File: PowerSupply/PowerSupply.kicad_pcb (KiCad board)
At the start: 2 copper layers, 100 x 58 mm, 26 parts, among them J1 AC+, J2 AC-, J3 POWER, U1 LM317_SOT-223, U2 LM337_SOT223

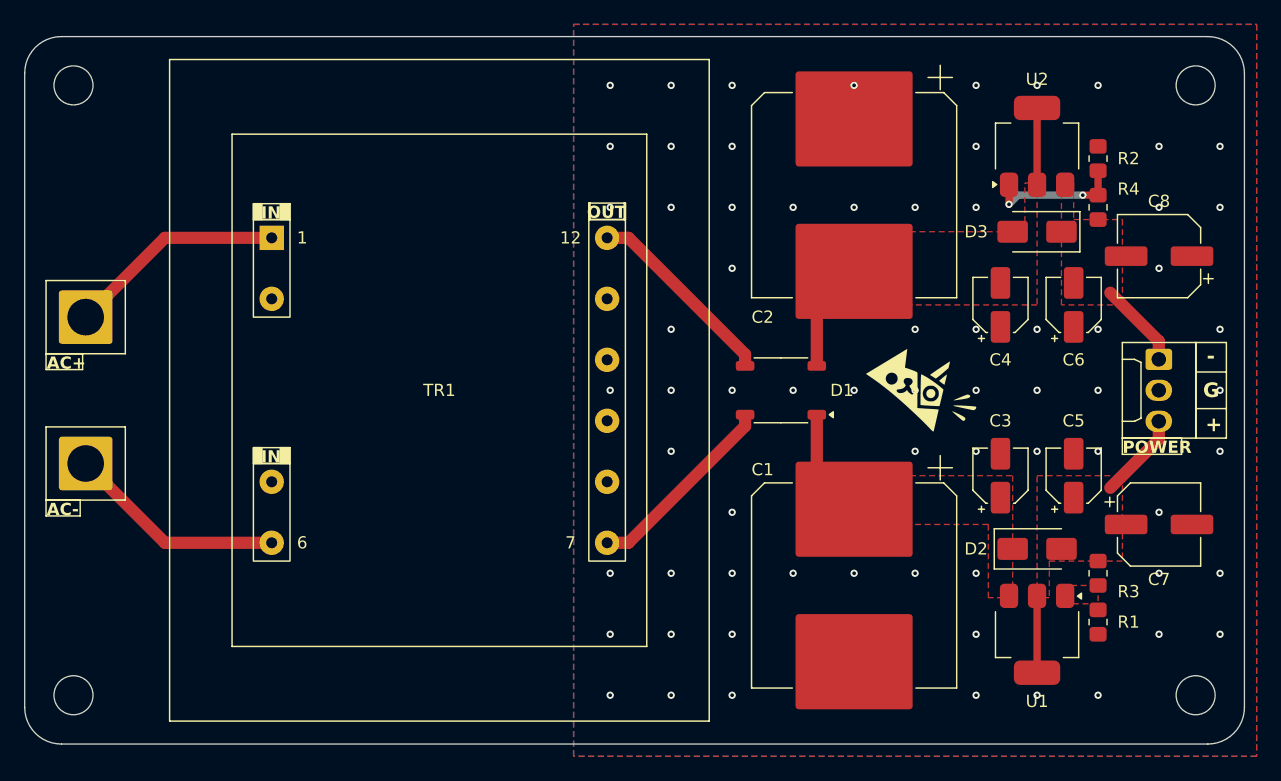
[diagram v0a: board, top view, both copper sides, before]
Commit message: Board Designs
Updated the power supply board design.
Updated the preamplifier board design.
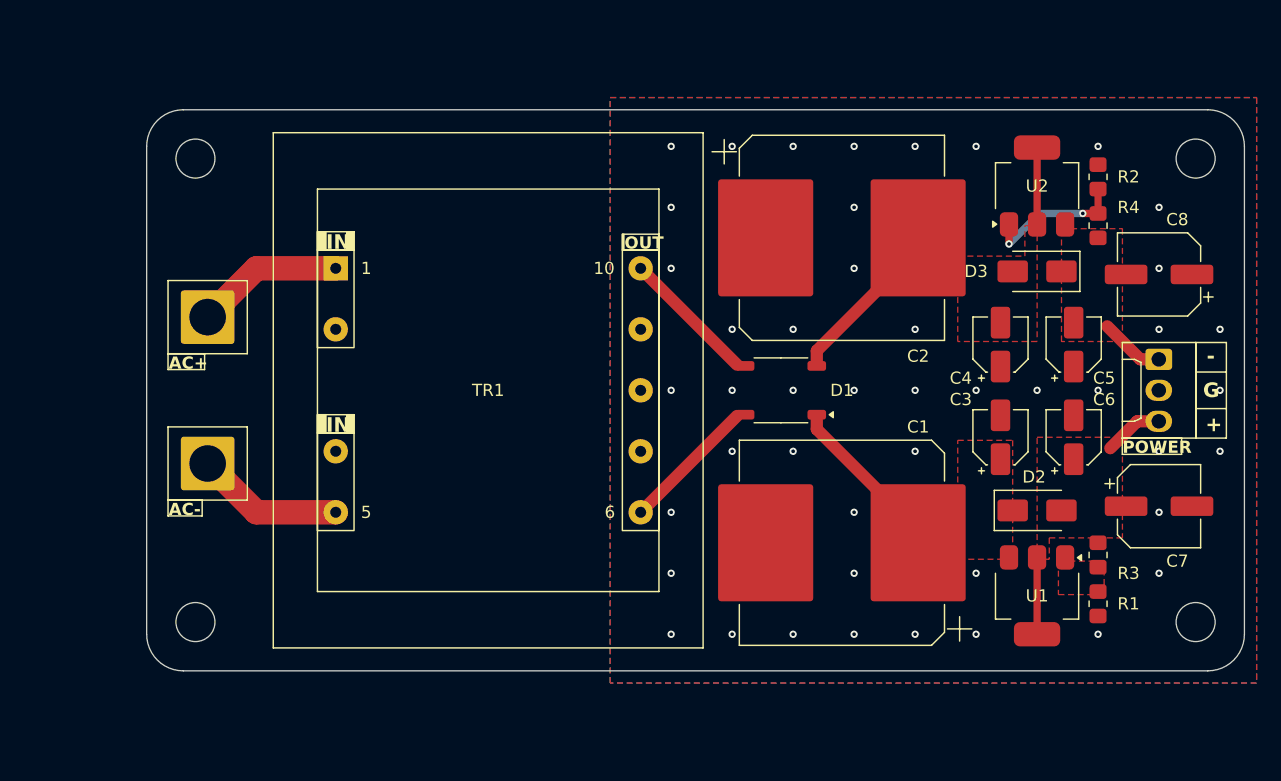
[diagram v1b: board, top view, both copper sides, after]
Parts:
- removed the G*** at (160.5, 100.0)
- added G***: LOGO, Logos:PowerSupply, B.Cu at (162.9, 100.0)
- added G***: LOGO, Logos:HighVoltage, B.Cu at (121.4, 98.7)
- TR1: value TEZ10.0-D-2 -> TEZ1.5-D-2; footprint Custom_Parts:TRANSFORMER_TEZ-44X52 -> Custom_Parts:TRANSFORMER_TEZ-35X42
- moved H1 11.7 mm to (101.0, 81.0)
- moved H2 11.7 mm to (101.0, 119.0)
- moved J1 10.0 mm to (102.0, 94.0)
- moved J2 10.0 mm to (102.0, 106.0)
- moved H3 6.00 mm to (183.0, 81.0)
- moved H4 6.00 mm to (183.0, 119.0)
- moved TR1 5.81 mm to (112.5, 90.0)
- moved C1 3.64 mm to (154.0, 112.5), turned to 180 degrees
- moved C2 3.64 mm to (154.0, 87.5), turned to 0 degrees
- moved C4 3.25 mm to (167.0, 96.2)
- moved C6 3.25 mm to (173.0, 96.2)
- moved D3 3.25 mm to (170.0, 90.2)
- moved U2 3.25 mm to (170.0, 83.2)
- moved C3 3.15 mm to (167.0, 103.8)
- moved C5 3.15 mm to (173.0, 103.8)
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- renumbered H3 to H2, H2 to H3
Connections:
- TR1 pad 10: (no net) -> Net-(D1-Pad3)
- TR1 pad 5: (no net) -> Net-(J2-Pin_1)
- TR1 pad 6: Net-(J2-Pin_1) -> Net-(D1-Pad4)
- TR1 pad 7: Net-(D1-Pad4) -> GND
- TR1 pad 8: GND -> (no net)
- TR1 pad 9: (no net) -> GND
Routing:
- net Net-(J2-Pin_1): track 17.9 -> 12.2 mm
- net Net-(J1-Pin_1): track 17.9 -> 12.2 mm
- net +15V: track 8.82 -> 13.7 mm
- net Net-(D1-Pad4): track 16.0 -> 11.2 mm
- net Net-(D1-Pad3): track 16.0 -> 11.2 mm
- net -15V: track 15.1 -> 19.0 mm
- net +12V: track 13.4 -> 11.2 mm
- net -12V: track 7.11 -> 5.35 mm
- net Net-(U2-ADJ): track 11.2 -> 11.9 mm
- net GND: vias 69 -> 46
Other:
- board size 100 x 58 mm -> 90 x 46 mm
- board text added: "V1.0"
- board text removed: "POWER SUPPLY"
- board text removed: "VERSION 1.0"

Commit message: Board Designs
Updated the power supply board design.
Updated the preamplifier board design.
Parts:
- moved G*** 1.06 mm to (122.1, 99.5)
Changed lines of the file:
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@@
 	(footprint "Logos:HighVoltage"
 		(layer "B.Cu")
-		(at 121.355046 98.748893 -90)
+		(at 122.105046 99.498893 -90)
 		(property "Reference" "G***"
 			(at 0 0 90)
